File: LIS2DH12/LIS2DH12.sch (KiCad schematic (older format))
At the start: 25 parts, among them J1 Conn_01x06, J2 Conn_01x04, J3 Conn_01x06, J4 Conn_01x04, Q1 BSS138DW, Q2 BSS138DW, U1 AP2127K-3.3

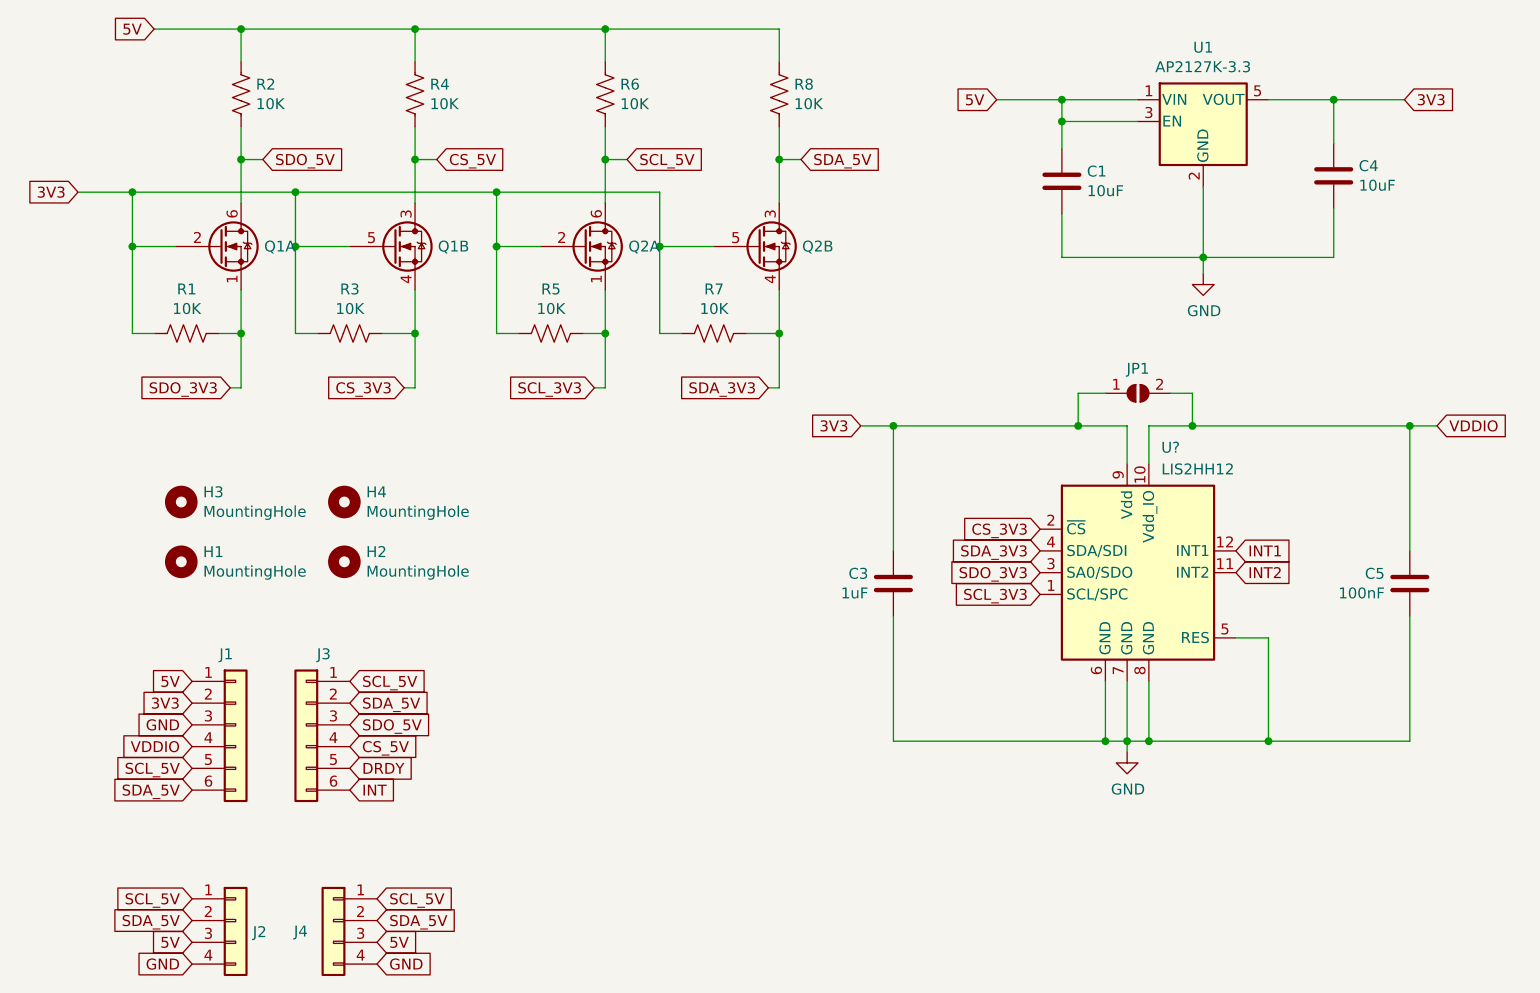
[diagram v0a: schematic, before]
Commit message: Schematic.pdf added for LIS2DH12
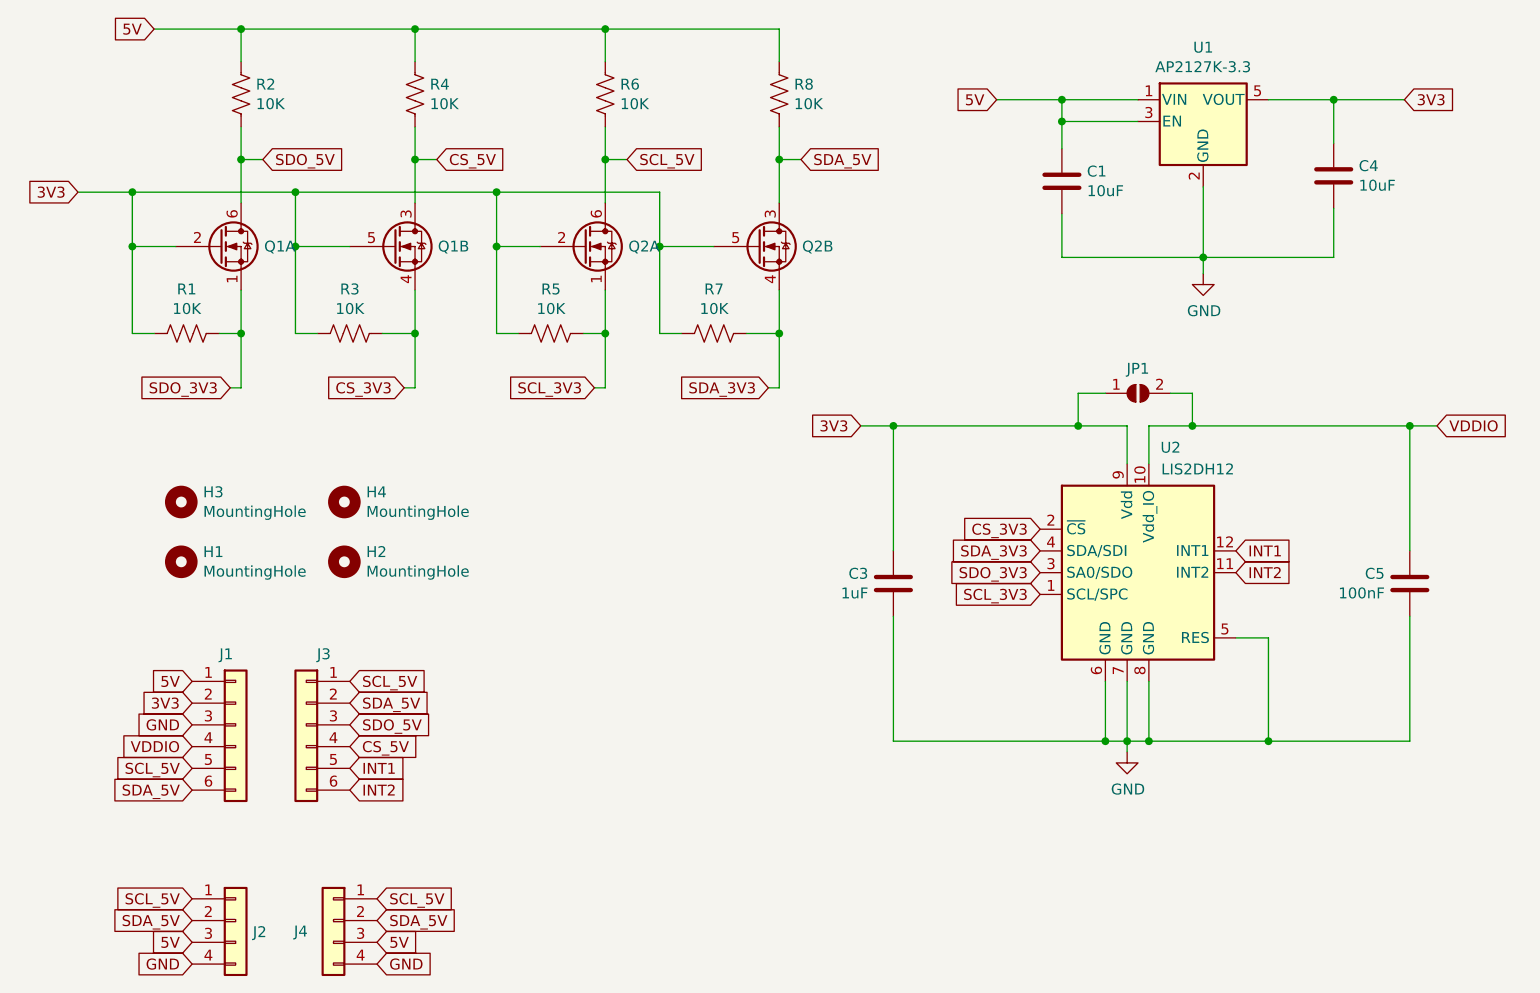
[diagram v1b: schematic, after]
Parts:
- U2: renamed from U?; value LIS2HH12 -> LIS2DH12
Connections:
- net DRDY is gone; now on net INT1: J3.5 (Pin_5)
- net INT is gone; now on net INT2: J3.6 (Pin_6)
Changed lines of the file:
@@
 $EndComp
 Text GLabel 1975 4125 2    50   Input ~ 0
-INT
+INT2
 Text GLabel 1250 3825 0    50   Input ~ 0
 GND
@@
 VDDIO
 Text GLabel 1975 4025 2    50   Input ~ 0
-DRDY
+INT1
 $Comp
 L Connector_Generic:Conn_01x04 J2
@@
 INT2
 $Comp
-L Sensor_Motion:LIS2HH12 U?
+L Sensor_Motion:LIS2HH12 U2
 U 1 1 5E709889
 P 5550 3125
-F 0 "U?" H 5750 3700 50  0000 C CNN
-F 1 "LIS2HH12" H 5875 3600 50  0000 C CNN
+F 0 "U2" H 5750 3700 50  0000 C CNN
+F 1 "LIS2DH12" H 5875 3600 50  0000 C CNN
 F 2 "Package_LGA:LGA-12_2x2mm_P0.5mm" H 5700 3675 50  0001 L CNN
 F 3 "www.st.com/resource/en/datasheet/lis2hh12.pdf" H 5200 3125 50  0001 C CNN

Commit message: Part Numbers Added
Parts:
- U2: Part (none) -> C110926
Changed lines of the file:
@@
 F 2 "Package_LGA:LGA-12_2x2mm_P0.5mm" H 5700 3675 50  0001 L CNN
 F 3 "www.st.com/resource/en/datasheet/lis2hh12.pdf" H 5200 3125 50  0001 C CNN
+F 4 "C110926" H 5550 3125 50  0001 C CNN "Part"
 	1    5550 3125
 	1    0    0    -1
